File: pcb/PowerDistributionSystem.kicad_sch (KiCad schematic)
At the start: 42 parts, among them J1 Pin-Out, J2 JST-PH, J3 JST-PH, J4 JST-PH, J5 JST-PH, J6 JST-PH, U1 D24V7F5, U2 D24V7F3, U6 TPS22810DRV

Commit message: Updated `StackConnector` to use reference prefix of "J".
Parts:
- renumbered C25 to J1, J2 to J1, J3 to J2, J4 to J3, J5 to J4, J6 to J5, J1 to J6, U6 to U1, U1 to U2, U2 to U3

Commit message: Using JST-PA connectors.
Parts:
- removed H1, H10, H11, H12, H13, H14, H15, H16, H2, H3, H4, H5, H6, H7, H8, H9: MountingHole_Pad_MP, pcb:Matrix_Hole, symbol Mechanical:MountingHole_Pad_MP
- removed J1: JST-PH, Connector_JST:JST_PH_B2B-PH-K_1x02_P2.00mm_Vertical, symbol Connector_Generic:Conn_01x02
- removed J5: JST-PH, Connector_JST:JST_PH_B8B-PH-K_1x08_P2.00mm_Vertical, symbol Connector_Generic:Conn_01x08
- removed J6: Pin-Out, Connector_IDC:IDC-Header_2x17_P2.54mm_Vertical, symbol Connector_Generic:Conn_02x17_Odd_Even
- removed N1: Housing, pcb:PowerDistributionSystemHousing, symbol Mechanical:Housing
- added J1, J5, J8: S04B-PASK-2, pcb:S04B-PASK-2, symbol Connector_Generic:Conn_01x04
- J2, J3, J4: value JST-PH -> S04B-PASK-2; footprint Connector_JST:JST_PH_B4B-PH-K_1x04_P2.00mm_Vertical -> pcb:S04B-PASK-2
- renumbered J1 to J7
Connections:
- net +BATT: now also J5.3 (Pin_3)
- net +EXTERNAL_A: now also J4.1 (Pin_1)
- net +EXTERNAL_B: now also J4.3 (Pin_3)
- net +EXTERNAL_C: now also J5.1 (Pin_1)
- net BURNWIRE_VOLTAGE: now also J8.1 (Pin_1), J8.3 (Pin_3)
- net GND: now also J4.2 (Pin_2), J4.4 (Pin_4), J5.2 (Pin_2), J5.4 (Pin_4), J8.2 (Pin_2), J8.4 (Pin_4)
- net MOTOR_DRIVER_A1_X: now also J1.1 (Pin_1); no longer J2.1 (Pin_1)
- net MOTOR_DRIVER_A1_Y: now also J2.1 (Pin_1); no longer J3.1 (Pin_1)
- net MOTOR_DRIVER_A1_Z: now also J3.1 (Pin_1); no longer J4.1 (Pin_1)
- net MOTOR_DRIVER_A2_X: now also J1.2 (Pin_2); no longer J2.2 (Pin_2)
- net MOTOR_DRIVER_A2_Y: now also J2.2 (Pin_2); no longer J3.2 (Pin_2)
- net MOTOR_DRIVER_A2_Z: now also J3.2 (Pin_2); no longer J4.2 (Pin_2)
- net MOTOR_DRIVER_B1_X: now also J1.3 (Pin_3); no longer J2.3 (Pin_3)
- net MOTOR_DRIVER_B1_Y: now also J2.3 (Pin_3); no longer J3.3 (Pin_3)
- net MOTOR_DRIVER_B1_Z: now also J3.3 (Pin_3); no longer J4.3 (Pin_3)
- net MOTOR_DRIVER_B2_X: now also J1.4 (Pin_4); no longer J2.4 (Pin_4)
- net MOTOR_DRIVER_B2_Y: now also J2.4 (Pin_4); no longer J3.4 (Pin_4)
- net MOTOR_DRIVER_B2_Z: now also J3.4 (Pin_4); no longer J4.4 (Pin_4)
- no-connect marks 108 -> 104
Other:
- note removed: "TODO: Uncertain about JST-PH connector."
- moved on the sheet: J7, JP1, JP2, R1, R2, R3, R4, RV1, TP1, TP2, TP3, TP4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

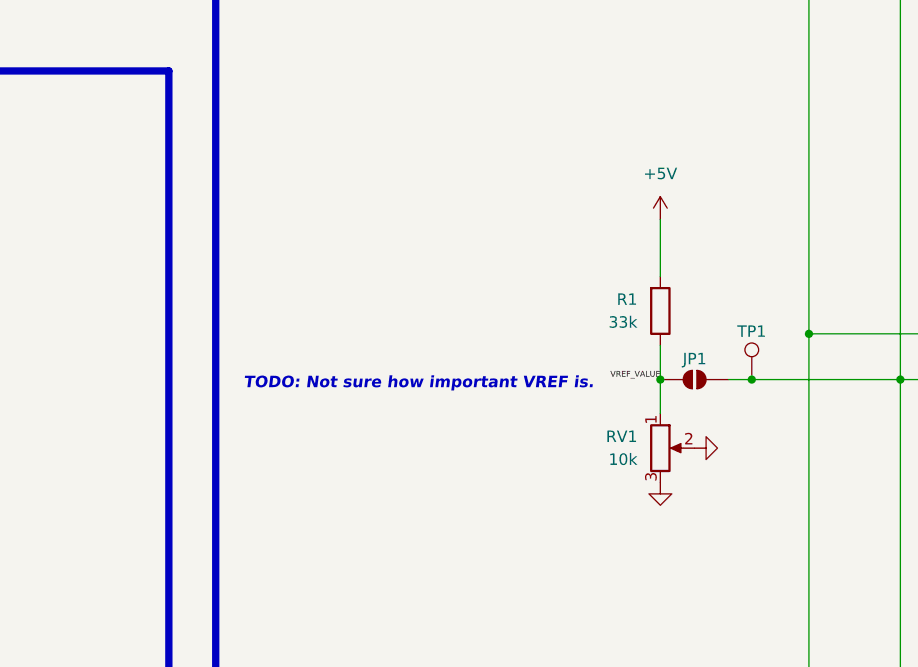
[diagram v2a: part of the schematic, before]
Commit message: Removed potentiometer for VREF.
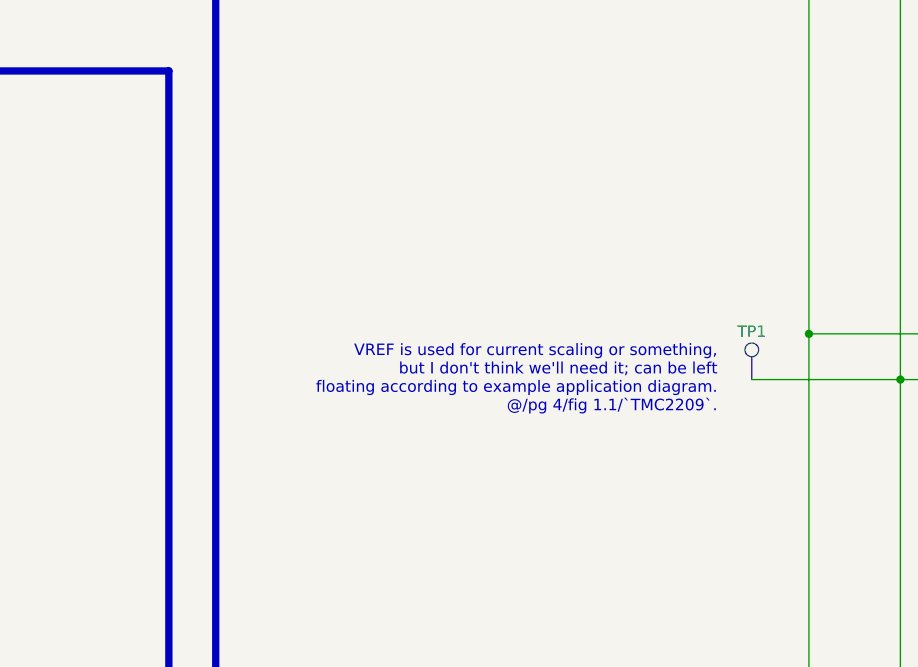
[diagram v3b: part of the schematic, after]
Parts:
- removed JP1: SolderJumper_2_Open, Jumper:SolderJumper-2_P1.3mm_Open_RoundedPad1.0x1.5mm, symbol Jumper:SolderJumper_2_Open
- removed R1: 33k, Resistor_SMD:R_1206_3216Metric_Pad1.30x1.75mm_HandSolder, symbol Device:R
- removed RV1: 10k, pcb:TRIM_35WR10KLFTR, symbol Device:R_Potentiometer
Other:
- note added: "VREF is used for current scaling or something, but I don't think we'll need it; can be left floating according to example application diagram. @/pg 4/fig 1.1/`TMC2209`."
- note removed: "TODO: Not sure how important VREF is."

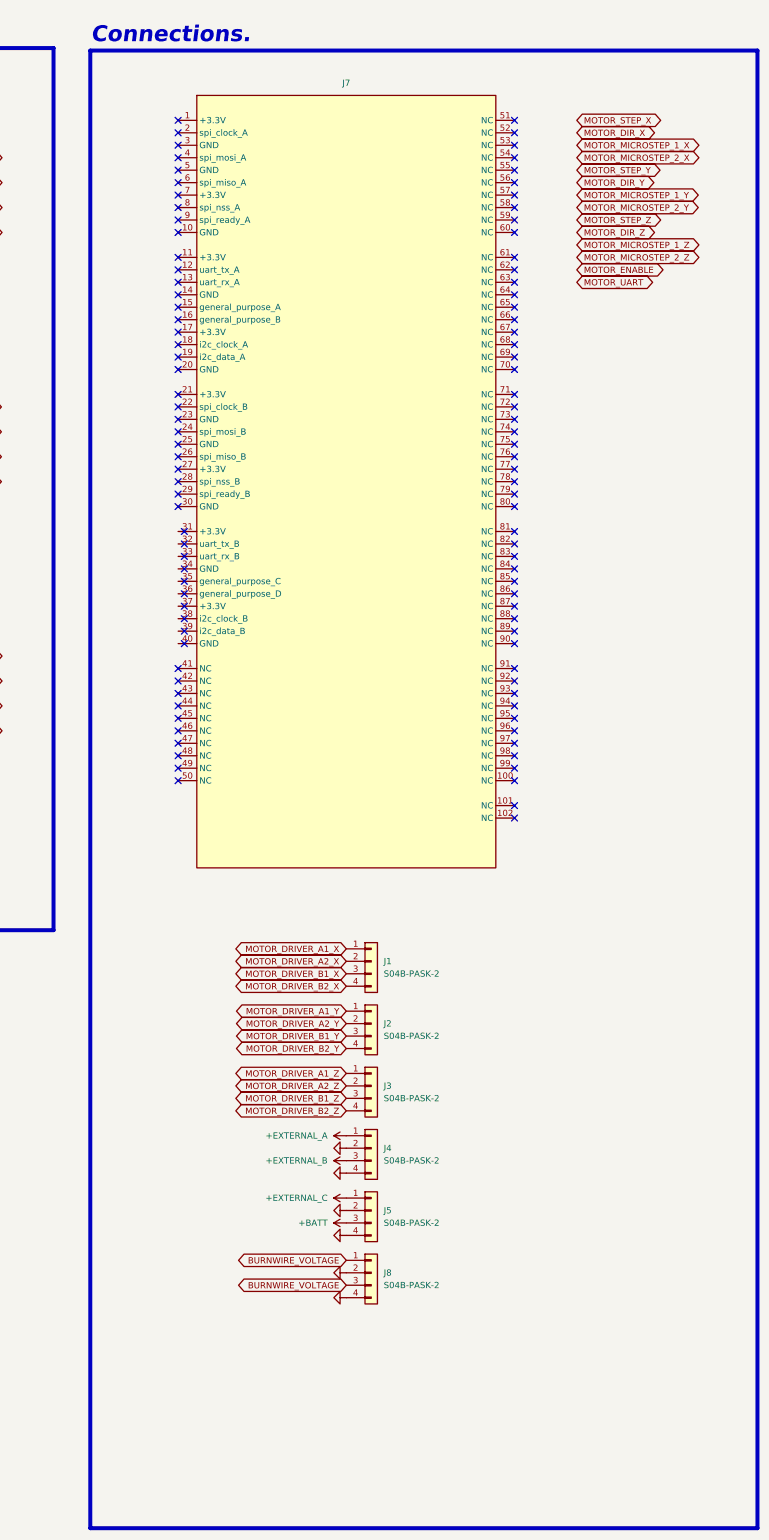
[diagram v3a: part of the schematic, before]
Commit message: Instead of S04B-PASK-2 connectors, regular 2.54mm horizontal pin headers will be used.
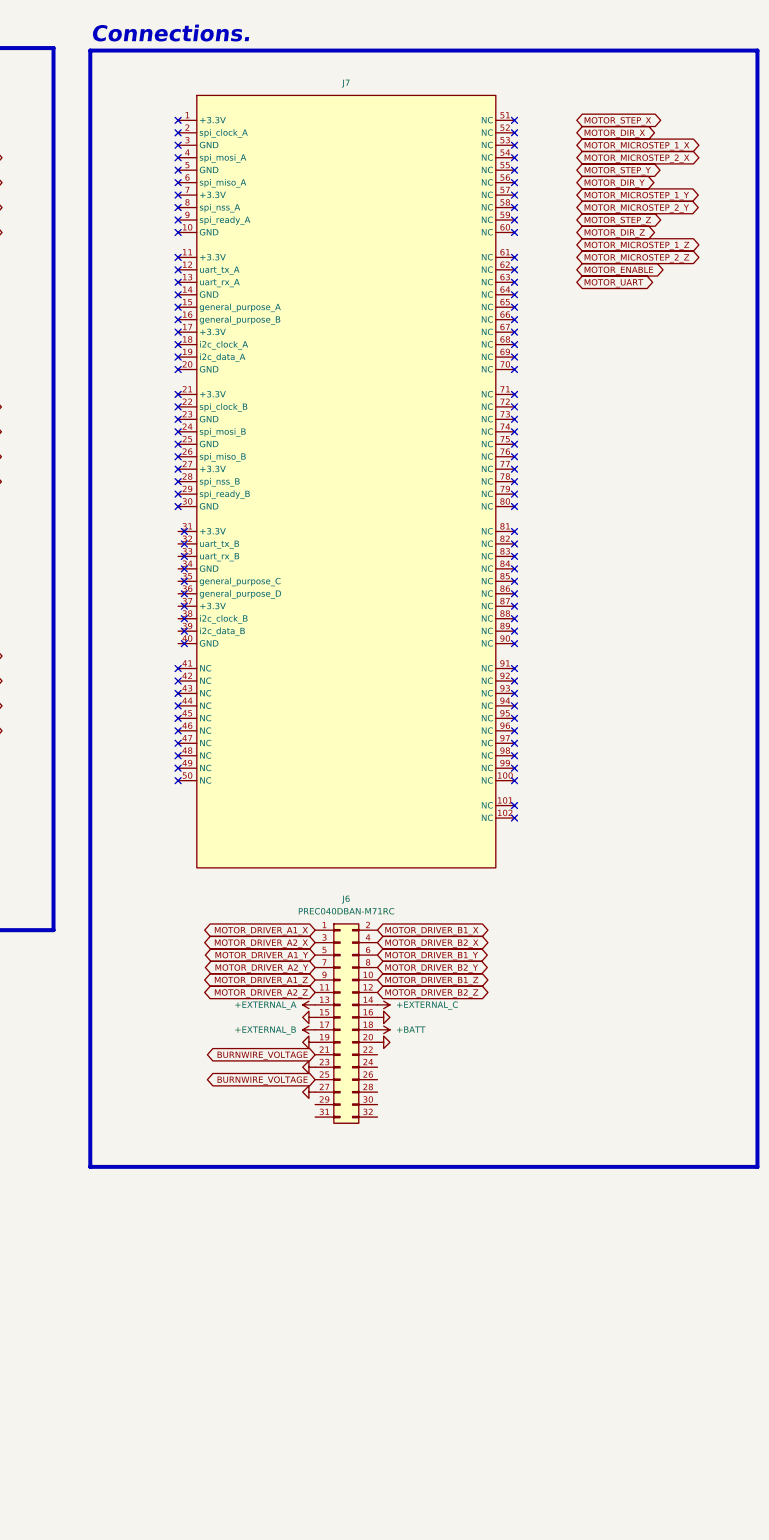
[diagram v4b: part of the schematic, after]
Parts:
- removed J1, J2, J3, J4, J5, J8: S04B-PASK-2, pcb:S04B-PASK-2, symbol Connector_Generic:Conn_01x04
- added J6: PREC040DBAN-M71RC, Connector_PinHeader_2.54mm:PinHeader_2x16_P2.54mm_Horizontal, symbol Connector_Generic:Conn_02x16_Odd_Even
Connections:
- net +BATT: now also J6.18 (Pin_18)
- net +EXTERNAL_A: now also J6.13 (Pin_13)
- net +EXTERNAL_B: now also J6.17 (Pin_17)
- net +EXTERNAL_C: now also J6.14 (Pin_14)
- net BURNWIRE_VOLTAGE: now also J6.21 (Pin_21), J6.25 (Pin_25)
- net GND: now also J6.15 (Pin_15), J6.16 (Pin_16), J6.19 (Pin_19), J6.20 (Pin_20), J6.23 (Pin_23), J6.27 (Pin_27)
- net MOTOR_DRIVER_A1_X: now also J6.1 (Pin_1)
- net MOTOR_DRIVER_A1_Y: now also J6.5 (Pin_5)
- net MOTOR_DRIVER_A1_Z: now also J6.9 (Pin_9)
- net MOTOR_DRIVER_A2_X: now also J6.3 (Pin_3)
- net MOTOR_DRIVER_A2_Y: now also J6.7 (Pin_7)
- net MOTOR_DRIVER_A2_Z: now also J6.11 (Pin_11)
- net MOTOR_DRIVER_B1_X: now also J6.2 (Pin_2)
- net MOTOR_DRIVER_B1_Y: now also J6.6 (Pin_6)
- net MOTOR_DRIVER_B1_Z: now also J6.10 (Pin_10)
- net MOTOR_DRIVER_B2_X: now also J6.4 (Pin_4)
- net MOTOR_DRIVER_B2_Y: now also J6.8 (Pin_8)
- net MOTOR_DRIVER_B2_Z: now also J6.12 (Pin_12)

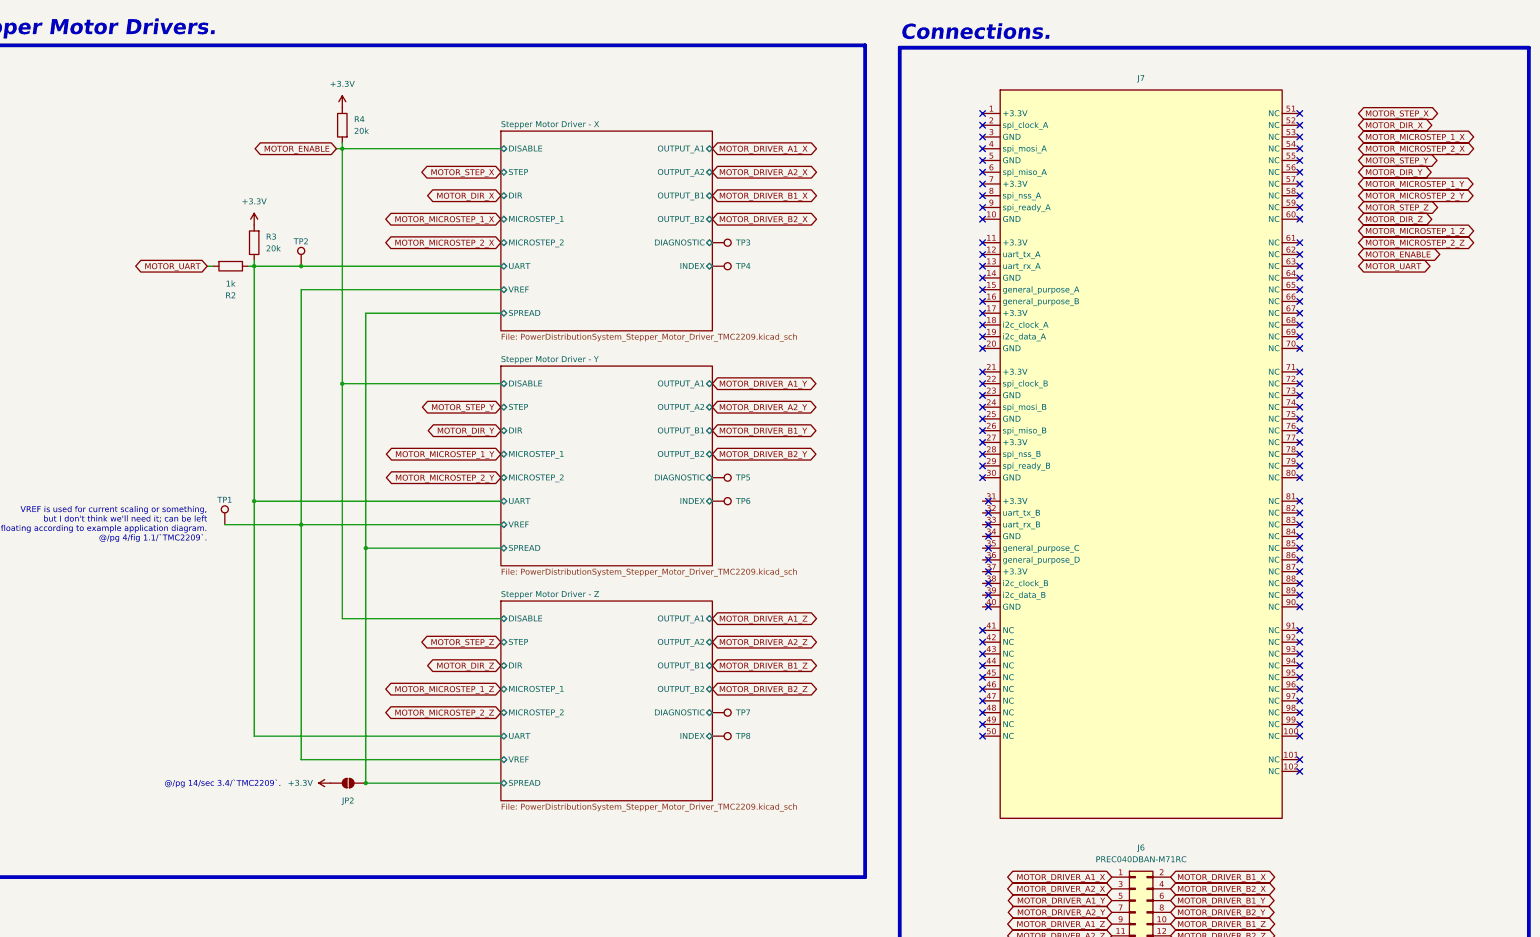
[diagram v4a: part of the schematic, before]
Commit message: Revised TMC2209 schematic.
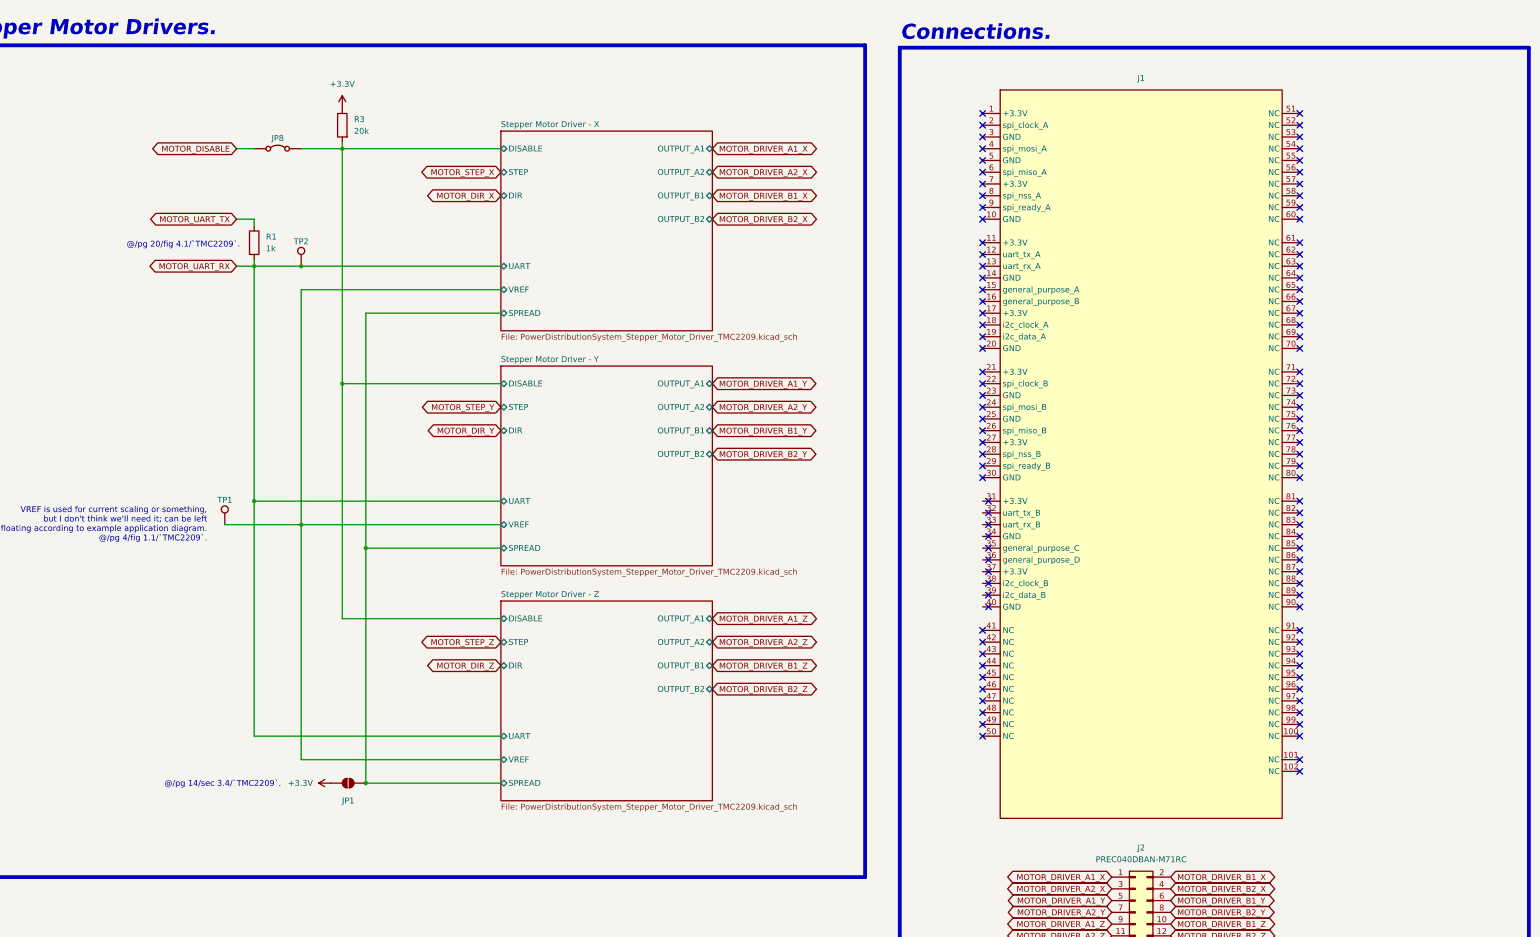
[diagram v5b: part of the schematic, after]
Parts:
- removed R3: 20k, Resistor_SMD:R_1206_3216Metric_Pad1.30x1.75mm_HandSolder, symbol Device:R
- removed TP3, TP4, TP5, TP6, TP7, TP8: TestPoint, TestPoint:TestPoint_Pad_1.0x1.0mm, symbol Connector:TestPoint
- added JP8: Jumper_2_Bridged, Jumper:SolderJumper-2_P1.3mm_Open_RoundedPad1.0x1.5mm, symbol Jumper:Jumper_2_Bridged
- renumbered J7 to J1, J6 to J2, JP2 to JP1, R2 to R1, R4 to R3
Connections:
- net MOTOR_ENABLE renamed Stepper Motor Driver - X/DISABLE
- net Stepper Motor Driver - X/DISABLE: now also JP8.2 (B)
- net MOTOR_UART renamed MOTOR_UART_RX
- net MOTOR_UART_RX: now also TP2.1
- net Stepper Motor Driver - X/UART renamed MOTOR_UART_TX
- net MOTOR_UART_TX: no longer TP2.1
- new net MOTOR_DISABLE: JP8.1 (A)
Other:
- sheet Stepper Motor Driver - X ports: added none; removed DIAGNOSTIC, INDEX, MICROSTEP_1, MICROSTEP_2
- sheet Stepper Motor Driver - Y ports: added none; removed DIAGNOSTIC, INDEX, MICROSTEP_1, MICROSTEP_2
- sheet Stepper Motor Driver - Z ports: added none; removed DIAGNOSTIC, INDEX, MICROSTEP_1, MICROSTEP_2
- note added: "@/pg 20/fig 4.1/`TMC2209`."
- moved on the sheet: R1
